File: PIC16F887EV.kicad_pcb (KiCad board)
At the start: 2 copper layers, 1 part, among them U1 PIC16F887-IP

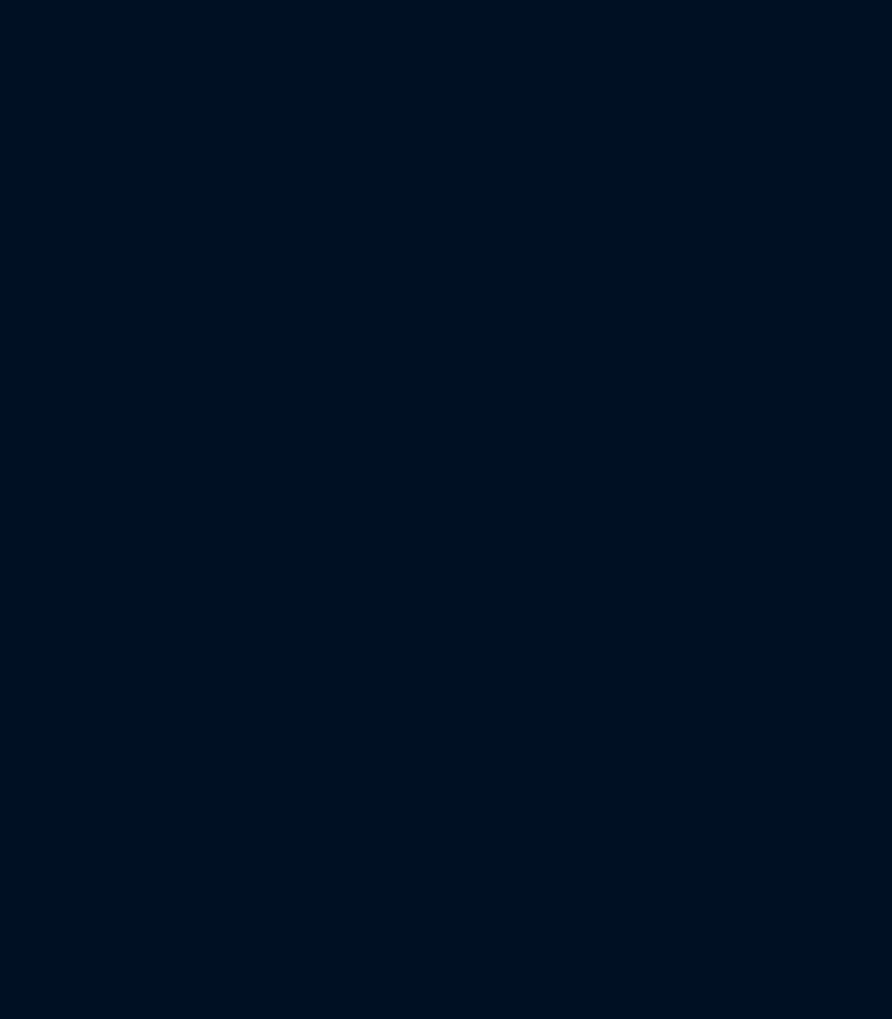
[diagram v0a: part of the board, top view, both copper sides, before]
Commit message: USB-C y FT230X
Agregado Puente USB y conector USB-C
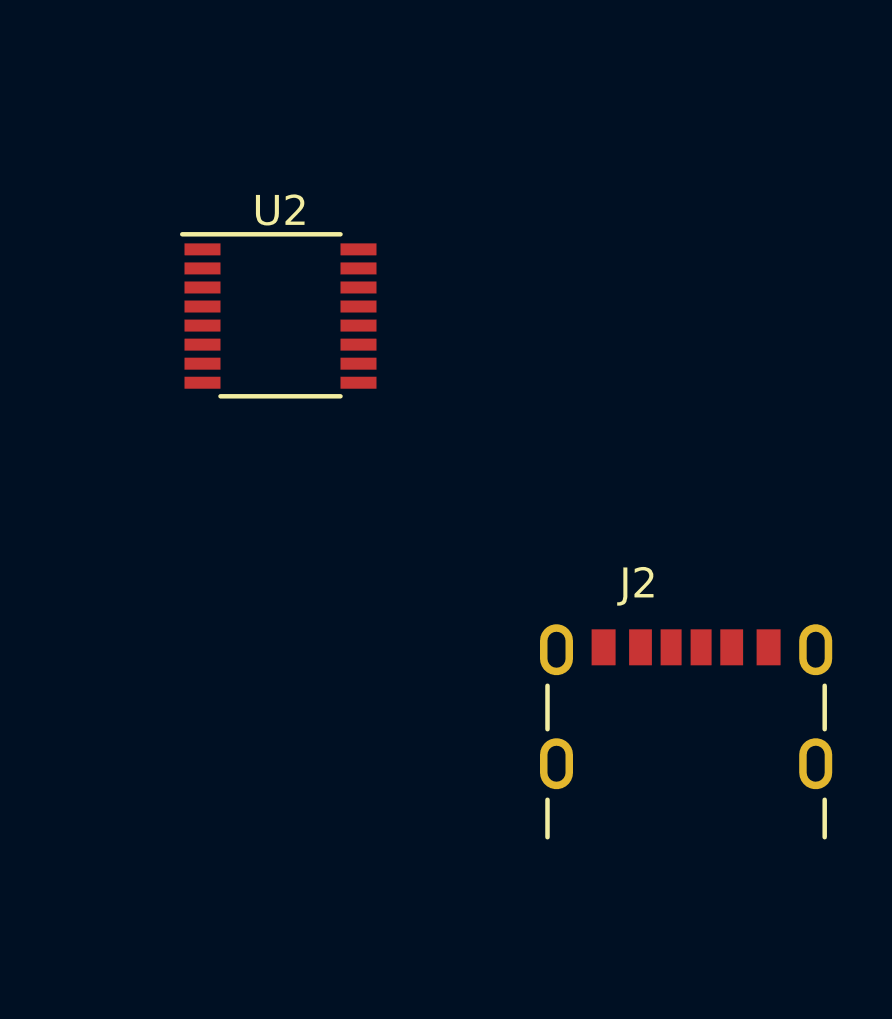
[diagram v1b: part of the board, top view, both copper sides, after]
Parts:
- added J2: 2171750001, usbc:MOLEX_2171750001, F.Cu at (186.2, 99.1)
- added U2: FT230XS, Package_SO:SSOP-16_3.9x4.9mm_P0.635mm, F.Cu at (172.7, 81.6)
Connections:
- U1 pad 1: unconnected-(U1-RE3/~{MCLR}/Vpp-Pad1) -> Net-(U1-RE2/AN7)
- U1 pad 10: unconnected-(U1-RE2/AN7-Pad10) -> Net-(U1-RE2/AN7)

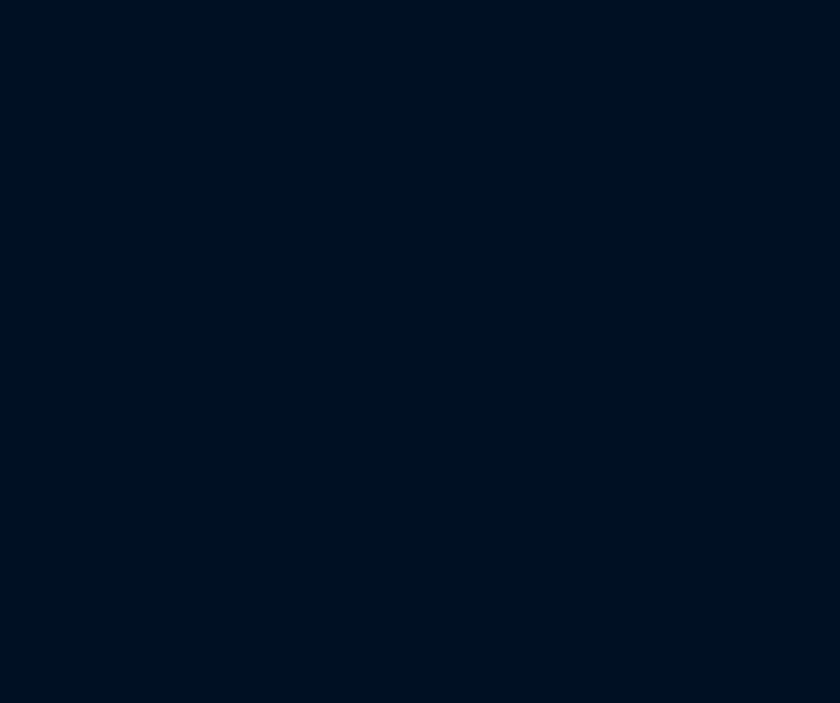
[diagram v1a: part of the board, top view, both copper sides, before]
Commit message: display SA56-11SRWA
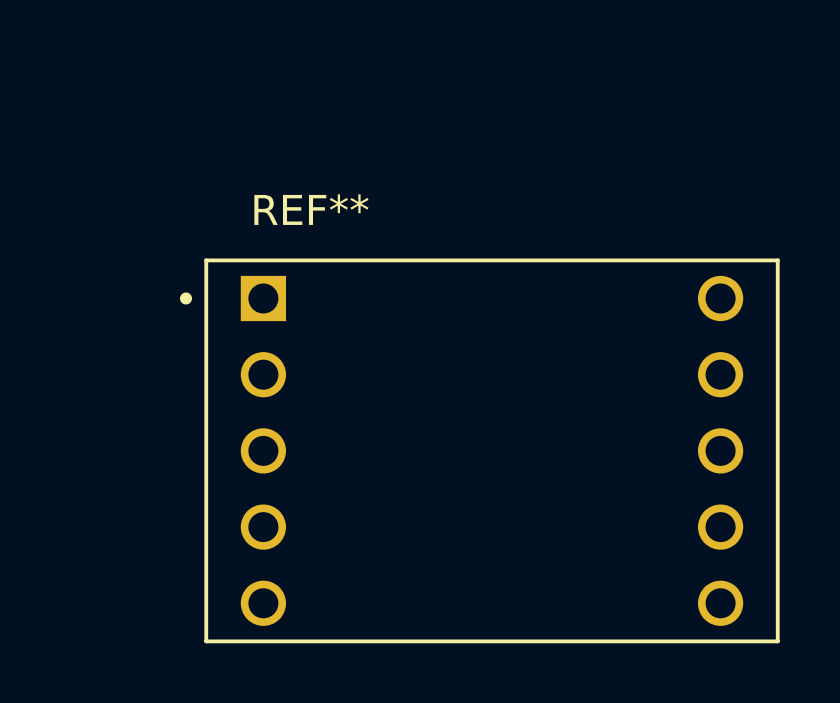
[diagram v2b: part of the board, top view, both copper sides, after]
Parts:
- added REF**: DISPLAY_SA56-11SRWA, Downloads:DISPLAY_SA56-11SRWA, F.Cu at (248.9, 106.7)
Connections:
- U1 pad 1: Net-(U1-RE2/AN7) -> unconnected-(U1-RE3/~{MCLR}/Vpp-Pad1)
- U1 pad 10: Net-(U1-RE2/AN7) -> unconnected-(U1-RE2/AN7-Pad10)
- U1 pad 19: unconnected-(U1-RD0-Pad19) -> RD0
- U1 pad 20: unconnected-(U1-RD1-Pad20) -> RD1
- U1 pad 21: unconnected-(U1-RD2-Pad21) -> RD2
- U1 pad 22: unconnected-(U1-RD3-Pad22) -> RD3
- U1 pad 33: unconnected-(U1-INT/AN12/RB0-Pad33) -> RB0
- U1 pad 34: unconnected-(U1-C12IN3-/AN10/RB1-Pad34) -> RB1
- U1 pad 35: unconnected-(U1-AN8/RB2-Pad35) -> RB2
- U1 pad 36: unconnected-(U1-C12IN2-/PGM/AN9/RB3-Pad36) -> RB3
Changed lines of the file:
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@@
   )
   (net 0 "")
-  (net 1 "Net-(U1-RE2{slash}AN7)")
+  (net 1 "unconnected-(U1-RE3{slash}~{MCLR}{slash}Vpp-Pad1)")
   (net 2 "unconnected-(U1-C12IN0-{slash}ULPWU{slash}AN0{slash}RA0-Pad2)")
   (net 3 "unconnected-(U1-C12IN1-{slash}AN1{slash}RA1-Pad3)")
@@
   (net 17 "unconnected-(U1-P1A{slash}CCP1{slash}RC2-Pad17)")
   (net 18 "unconnected-(U1-SCL{slash}SCK{slash}RC3-Pad18)")
-  (net 19 "unconnected-(U1-RD0-Pad19)")
-  (net 20 "unconnected-(U1-RD1-Pad20)")
-  (net 21 "unconnected-(U1-RD2-Pad21)")
-  (net 22 "unconnected-(U1-RD3-Pad22)")
+  (net 19 "unconnected-(U1-RE2{slash}AN7-Pad10)")
+  (net 20 "RD0")
+  (net 21 "RD1")
+  (net 22 "RD2")
   (net 23 "unconnected-(U1-SDA{slash}SDI{slash}RC4-Pad23)")
   (net 24 "unconnected-(U1-SDO{slash}RC5-Pad24)")
@@
   (net 31 "unconnected-(U1-VSS-Pad31)")
   (net 32 "unconnected-(U1-VDD-Pad32)")
-  (net 33 "unconnected-(U1-INT{slash}AN12{slash}RB0-Pad33)")
-  (net 34 "unconnected-(U1-C12IN3-{slash}AN10{slash}RB1-Pad34)")
-  (net 35 "unconnected-(U1-AN8{slash}RB2-Pad35)")
-  (net 36 "unconnected-(U1-C12IN2-{slash}PGM{slash}AN9{slash}RB3-Pad36)")
+  (net 33 "RD3")
+  (net 34 "RB0")
+  (net 35 "RB1")
+  (net 36 "RB2")
   (net 37 "unconnected-(U1-AN11{slash}RB4-Pad37)")
   (net 38 "unconnected-(U1-~{T1G}{slash}AN13{slash}RB5-Pad38)")
@@
   (net 64 "unconnected-(J2-SHIELD3-PadSH3)")
   (net 65 "unconnected-(J2-SHIELD4-PadSH4)")
+  (net 66 "RB3")
+  (footprint "Downloads:DISPLAY_SA56-11SRWA" (layer "F.Cu")
+    (at 248.92 106.68)
+    (attr through_hole)
+    (fp_text reference "REF**" (at -6.065 -7.995) (layer "F.SilkS")
+        (effects (font (size 1 1) (thickness 0.15)))
+    )
+    (fp_text value "DISPLAY_SA56-11SRWA" (at 2.825 7.355) (layer "F.Fab")
+        (effects (font (size 1 1) (thickness 0.15)))
+    )
+    (fp_line (start -9.525 -6.35) (end 9.525 -6.35)
+      (stroke (width 0.127) (type solid)) (layer "F.SilkS"))
+    (fp_line (start -9.525 6.35) (end -9.525 -6.35)
+      (stroke (width 0.127) (type solid)) (layer "F.SilkS"))
+    (fp_line (start 9.525 -6.35) (end 9.525 6.35)
+      (stroke (width 0.127) (type solid)) (layer "F.SilkS"))
+    (fp_line (start 9.525 6.35) (end -9.525 6.35)
+      (stroke (width 0.127) (type solid)) (layer "F.SilkS"))
+    (fp_circle (center -10.2 -5.08) (end -10.1 -5.08)
+      (stroke (width 0.2) (type solid)) (fill none) (layer "F.SilkS"))
+    (fp_line (start -9.775 -6.6) (end 9.775 -6.6)
+      (stroke (width 0.05) (type solid)) (layer "F.CrtYd"))
+    (fp_line (start -9.775 6.6) (end -9.775 -6.6)
+      (stroke (width 0.05) (type solid)) (layer "F.CrtYd"))
+    (fp_line (start 9.775 -6.6) (end 9.775 6.6)
+      (stroke (width 0.05) (type solid)) (layer "F.CrtYd"))
+    (fp_line (start 9.775 6.6) (end -9.775 6.6)
+      (stroke (width 0.05) (type solid)) (layer "F.CrtYd"))
+    (fp_line (start -9.525 -6.35) (end 9.525 -6.35)
+      (stroke (width 0.127) (type solid)) (layer "F.Fab"))
+    (fp_line (start -9.525 6.35) (end -9.525 -6.35)
+      (stroke (width 0.127) (type solid)) (layer "F.Fab"))
+    (fp_line (start 9.525 -6.35) (end 9.525 6.35)
+      (stroke (width 0.127) (type solid)) (layer "F.Fab"))
+    (fp_line (start 9.525 6.35) (end -9.525 6.35)
+      (stroke (width 0.127) (type solid)) (layer "F.Fab"))
+    (fp_circle (center -10.2 -5.08) (end -10.1 -5.08)
+      (stroke (width 0.2) (type solid)) (fill none) (layer "F.Fab"))
+    (pad "1" thru_hole rect (at -7.62 -5.08) (size 1.508 1.508) (drill 1) (layers "*.Cu" "*.Mask")
+      (solder_mask_margin 0.102))
+    (pad "2" thru_hole circle (at -7.62 -2.54) (size 1.508 1.508) (drill 1) (layers "*.Cu" "*.Mask")
+      (solder_mask_margin 0.102))
+    (pad "3" thru_hole circle (at -7.62 0) (size 1.508 1.508) (drill 1) (layers "*.Cu" "*.Mask")
+      (solder_mask_margin 0.102))
+    (pad "4" thru_hole circle (at -7.62 2.54) (size 1.508 1.508) (drill 1) (layers "*.Cu" "*.Mask")
+      (solder_mask_margin 0.102))
+    (pad "5" thru_hole circle (at -7.62 5.08) (size 1.508 1.508) (drill 1) (layers "*.Cu" "*.Mask")
+      (solder_mask_margin 0.102))
+    (pad "6" thru_hole circle (at 7.62 5.08) (size 1.508 1.508) (drill 1) (layers "*.Cu" "*.Mask")
+      (solder_mask_margin 0.102))
+    (pad "7" thru_hole circle (at 7.62 2.54) (size 1.508 1.508) (drill 1) (layers "*.Cu" "*.Mask")
+      (solder_mask_margin 0.102))
+    (pad "8" thru_hole circle (at 7.62 0) (size 1.508 1.508) (drill 1) (layers "*.Cu" "*.Mask")
+      (solder_mask_margin 0.102))
+    (pad "9" thru_hole circle (at 7.62 -2.54) (size 1.508 1.508) (drill 1) (layers "*.Cu" "*.Mask")
+      (solder_mask_margin 0.102))
+    (pad "10" thru_hole circle (at 7.62 -5.08) (size 1.508 1.508) (drill 1) (layers "*.Cu" "*.Mask")
+      (solder_mask_margin 0.102))
+  )
   (footprint "Package_DIP:DIP-40_W15.24mm_LongPads" (layer "F.Cu")
     (at 129.54 55.88)
@@
       (stroke (width 0.1) (type solid)) (layer "F.Fab"))
     (pad "1" thru_hole rect (at 0 0) (size 2.4 1.6) (drill 0.8) (layers "*.Cu" "*.Mask")
-      (net 1 "Net-(U1-RE2{slash}AN7)") (pinfunction "RE3/~{MCLR}/Vpp") (pintype "input"))
+      (net 1 "unconnected-(U1-RE3{slash}~{MCLR}{slash}Vpp-Pad1)") (pinfunction "RE3/~{MCLR}/Vpp") (pintype "input"))
     (pad "2" thru_hole oval (at 0 2.54) (size 2.4 1.6) (drill 0.8) (layers "*.Cu" "*.Mask")
       (net 2 "unconnected-(U1-C12IN0-{slash}ULPWU{slash}AN0{slash}RA0-Pad2)") (pinfunction "C12IN0-/ULPWU/AN0/RA0") (pintype "bidirectional"))
@@
       (net 9 "unconnected-(U1-RE1{slash}AN6-Pad9)") (pinfunction "RE1/AN6") (pintype "bidirectional"))
     (pad "10" thru_hole oval (at 0 22.86) (size 2.4 1.6) (drill 0.8) (layers "*.Cu" "*.Mask")
-      (net 1 "Net-(U1-RE2{slash}AN7)") (pinfunction "RE2/AN7") (pintype "bidirectional"))
+      (net 19 "unconnected-(U1-RE2{slash}AN7-Pad10)") (pinfunction "RE2/AN7") (pintype "bidirectional"))
     (pad "11" thru_hole oval (at 0 25.4) (size 2.4 1.6) (drill 0.8) (layers "*.Cu" "*.Mask")
       (net 11 "unconnected-(U1-VDD-Pad11)") (pinfunction "VDD") (pintype "power_in"))
@@
       (net 18 "unconnected-(U1-SCL{slash}SCK{slash}RC3-Pad18)") (pinfunction "SCL/SCK/RC3") (pintype "bidirectional"))
     (pad "19" thru_hole oval (at 0 45.72) (size 2.4 1.6) (drill 0.8) (layers "*.Cu" "*.Mask")
-      (net 19 "unconnected-(U1-RD0-Pad19)") (pinfunction "RD0") (pintype "bidirectional"))
+      (net 20 "RD0") (pinfunction "RD0") (pintype "bidirectional"))
     (pad "20" thru_hole oval (at 0 48.26) (size 2.4 1.6) (drill 0.8) (layers "*.Cu" "*.Mask")
-      (net 20 "unconnected-(U1-RD1-Pad20)") (pinfunction "RD1") (pintype "bidirectional"))
+      (net 21 "RD1") (pinfunction "RD1") (pintype "bidirectional"))
     (pad "21" thru_hole oval (at 15.24 48.26) (size 2.4 1.6) (drill 0.8) (layers "*.Cu" "*.Mask")
-      (net 21 "unconnected-(U1-RD2-Pad21)") (pinfunction "RD2") (pintype "bidirectional"))
+      (net 22 "RD2") (pinfunction "RD2") (pintype "bidirectional"))
     (pad "22" thru_hole oval (at 15.24 45.72) (size 2.4 1.6) (drill 0.8) (layers "*.Cu" "*.Mask")
-      (net 22 "unconnected-(U1-RD3-Pad22)") (pinfunction "RD3") (pintype "bidirectional"))
+      (net 33 "RD3") (pinfunction "RD3") (pintype "bidirectional"))
     (pad "23" thru_hole oval (at 15.24 43.18) (size 2.4 1.6) (drill 0.8) (layers "*.Cu" "*.Mask")
       (net 23 "unconnected-(U1-SDA{slash}SDI{slash}RC4-Pad23)") (pinfunction "SDA/SDI/RC4") (pintype "bidirectional"))
@@
       (net 32 "unconnected-(U1-VDD-Pad32)") (pinfunction "VDD") (pintype "power_in"))
     (pad "33" thru_hole oval (at 15.24 17.78) (size 2.4 1.6) (drill 0.8) (layers "*.Cu" "*.Mask")
-      (net 33 "unconnected-(U1-INT{slash}AN12{slash}RB0-Pad33)") (pinfunction "INT/AN12/RB0") (pintype "bidirectional"))
+      (net 34 "RB0") (pinfunction "INT/AN12/RB0") (pintype "bidirectional"))
     (pad "34" thru_hole oval (at 15.24 15.24) (size 2.4 1.6) (drill 0.8) (layers "*.Cu" "*.Mask")
-      (net 34 "unconnected-(U1-C12IN3-{slash}AN10{slash}RB1-Pad34)") (pinfunction "C12IN3-/AN10/RB1") (pintype "bidirectional"))
+      (net 35 "RB1") (pinfunction "C12IN3-/AN10/RB1") (pintype "bidirectional"))
     (pad "35" thru_hole oval (at 15.24 12.7) (size 2.4 1.6) (drill 0.8) (layers "*.Cu" "*.Mask")
-      (net 35 "unconnected-(U1-AN8{slash}RB2-Pad35)") (pinfunction "AN8/RB2") (pintype "bidirectional"))
+      (net 36 "RB2") (pinfunction "AN8/RB2") (pintype "bidirectional"))
     (pad "36" thru_hole oval (at 15.24 10.16) (size 2.4 1.6) (drill 0.8) (layers "*.Cu" "*.Mask")
-      (net 36 "unconnected-(U1-C12IN2-{slash}PGM{slash}AN9{slash}RB3-Pad36)") (pinfunction "C12IN2-/PGM/AN9/RB3") (pintype "bidirectional"))
+      (net 66 "RB3") (pinfunction "C12IN2-/PGM/AN9/RB3") (pintype "bidirectional"))
     (pad "37" thru_hole oval (at 15.24 7.62) (size 2.4 1.6) (drill 0.8) (layers "*.Cu" "*.Mask")
       (net 37 "unconnected-(U1-AN11{slash}RB4-Pad37)") (pinfunction "AN11/RB4") (pintype "bidirectional"))

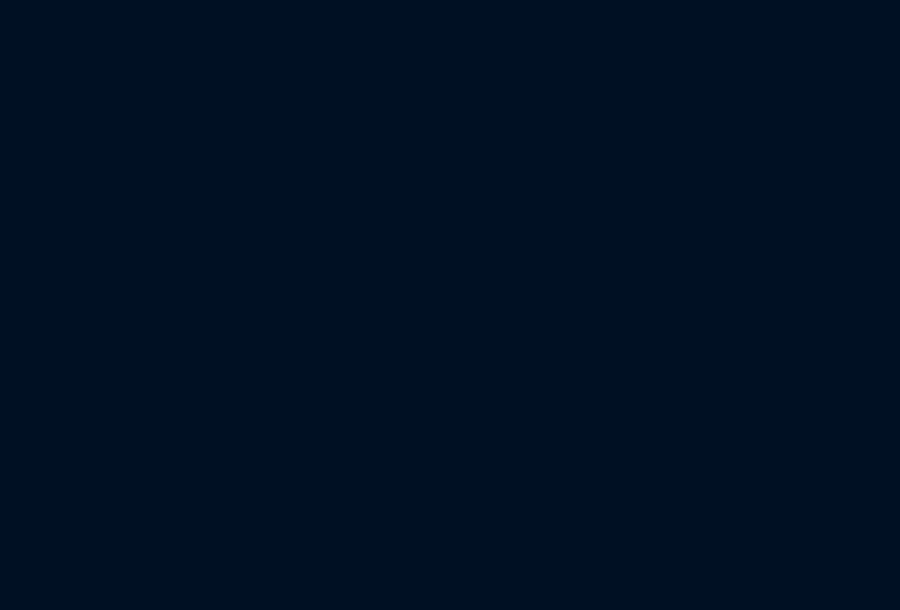
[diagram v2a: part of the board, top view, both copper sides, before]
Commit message: SW1 Huella
Cambio Botón SW1, ahora con huella
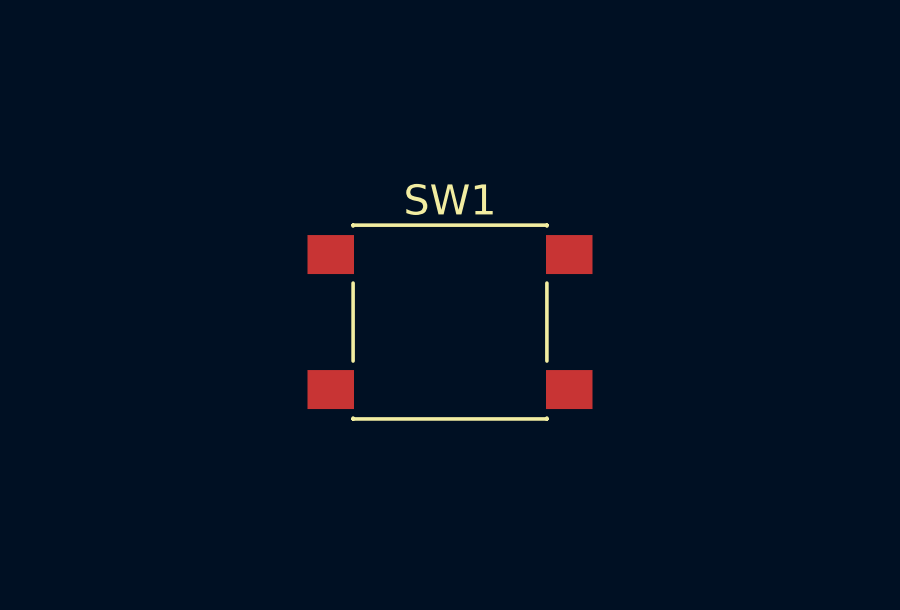
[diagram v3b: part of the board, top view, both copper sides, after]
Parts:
- added SW1: SW_Push, Button_Switch_SMD:SW_Push_1P1T_NO_6x6mm_H9.5mm, F.Cu at (181.4, 61.2)
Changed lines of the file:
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@@
   (net 65 "unconnected-(J2-SHIELD4-PadSH4)")
   (net 66 "RB3")
+  (footprint "Button_Switch_SMD:SW_Push_1P1T_NO_6x6mm_H9.5mm" (layer "F.Cu")
+    (at 181.445 61.25)
+    (descr "tactile push button, 6x6mm e.g. PTS645xx series, height=9.5mm")
+    (tags "tact sw push 6mm smd")
+    (property "Sheetfile" "PIC16F887EV.kicad_sch")
+    (property "Sheetname" "")
+    (property "ki_description" "Push button switch, generic, two pins")
+    (property "ki_keywords" "switch normally-open pushbutton push-button")
+    (attr smd)
+    (fp_text reference "SW1" (at 0 -4.05) (layer "F.SilkS")
+        (effects (font (size 1 1) (thickness 0.15)))
+    )
+    (fp_text value "SW_Push" (at 0 4.15) (layer "F.Fab")
+        (effects (font (size 1 1) (thickness 0.15)))
+    )
+    (fp_text user "${REFERENCE}" (at 0 -4.05) (layer "F.Fab")
+        (effects (font (size 1 1) (thickness 0.15)))
+    )
+    (fp_line (start -3.23 -3.23) (end 3.23 -3.23)
+      (stroke (width 0.12) (type solid)) (layer "F.SilkS"))
+    (fp_line (start -3.23 -3.2) (end -3.23 -3.23)
+      (stroke (width 0.12) (type solid)) (layer "F.SilkS"))
+    (fp_line (start -3.23 -1.3) (end -3.23 1.3)
+      (stroke (width 0.12) (type solid)) (layer "F.SilkS"))
+    (fp_line (start -3.23 3.23) (end -3.23 3.2)
+      (stroke (width 0.12) (type solid)) (layer "F.SilkS"))
+    (fp_line (start -3.23 3.23) (end 3.23 3.23)
+      (stroke (width 0.12) (type solid)) (layer "F.SilkS"))
+    (fp_line (start 3.23 -3.23) (end 3.23 -3.2)
+      (stroke (width 0.12) (type solid)) (layer "F.SilkS"))
+    (fp_line (start 3.23 -1.3) (end 3.23 1.3)
+      (stroke (width 0.12) (type solid)) (layer "F.SilkS"))
+    (fp_line (start 3.23 3.23) (end 3.23 3.2)
+      (stroke (width 0.12) (type solid)) (layer "F.SilkS"))
+    (fp_line (start -5 -3.25) (end -5 3.25)
+      (stroke (width 0.05) (type solid)) (layer "F.CrtYd"))
+    (fp_line (start -5 -3.25) (end 5 -3.25)
+      (stroke (width 0.05) (type solid)) (layer "F.CrtYd"))
+    (fp_line (start -5 3.25) (end 5 3.25)
+      (stroke (width 0.05) (type solid)) (layer "F.CrtYd"))
+    (fp_line (start 5 3.25) (end 5 -3.25)
+      (stroke (width 0.05) (type solid)) (layer "F.CrtYd"))
+    (fp_line (start -3 -3) (end -3 3)
+      (stroke (width 0.1) (type solid)) (layer "F.Fab"))
+    (fp_line (start -3 3) (end 3 3)
+      (stroke (width 0.1) (type solid)) (layer "F.Fab"))
+    (fp_line (start 3 -3) (end -3 -3)
+      (stroke (width 0.1) (type solid)) (layer "F.Fab"))
+    (fp_line (start 3 3) (end 3 -3)
+      (stroke (width 0.1) (type solid)) (layer "F.Fab"))
+    (fp_circle (center 0 0) (end 1.75 -0.05)
+      (stroke (width 0.1) (type solid)) (fill none) (layer "F.Fab"))
+    (pad "1" smd rect (at -3.975 -2.25) (size 1.55 1.3) (layers "F.Cu" "F.Paste" "F.Mask")
+      (net 20 "RD0") (pinfunction "1") (pintype "passive"))
+    (pad "1" smd rect (at 3.975 -2.25) (size 1.55 1.3) (layers "F.Cu" "F.Paste" "F.Mask")
+      (net 20 "RD0") (pinfunction "1") (pintype "passive"))
+    (pad "2" smd rect (at -3.975 2.25) (size 1.55 1.3) (layers "F.Cu" "F.Paste" "F.Mask")
+      (net 34 "RB0") (pinfunction "2") (pintype "passive"))
+    (pad "2" smd rect (at 3.975 2.25) (size 1.55 1.3) (layers "F.Cu" "F.Paste" "F.Mask")
+      (net 34 "RB0") (pinfunction "2") (pintype "passive"))
+    (model "${KICAD6_3DMODEL_DIR}/Button_Switch_SMD.3dshapes/SW_PUSH_6mm_H9.5mm.wrl"
+      (offset (xyz 0 0 0))
+      (scale (xyz 1 1 1))
+      (rotate (xyz 0 0 0))
+    )
+  )
   (footprint "Downloads:DISPLAY_SA56-11SRWA" (layer "F.Cu")
     (at 248.92 106.68)
